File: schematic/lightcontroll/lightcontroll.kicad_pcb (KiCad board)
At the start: 2 copper layers, 99.1 x 99.1 mm, 122 parts, among them J1 SPI1_SS, J10 SPI 5V, J11 3.3V jumper, J12 Header 24X2, J13 Header 24X2, J14 ATX24connector, J15 PWR_JMP, J16 PWR_JMP, J18 DB9_Female_MountingHoles, J19 SK2812_sig, J2 5V Selector, J20 SPI 5V, J21 RJ45_LED_Shielded, J22 Conn_01x03, J23 Conn_01x03, J24 Conn_01x03, J25 Conn_01x03, J26 SK2812_sig, J27 SPI1_MISO, J28 Conn_01x03, J29 Conn_01x03, J3 SPI1_CLK, J30 SK2812_sig, J31 SPI1_MOSI, J32 Conn_01x03, J33 SPI2_SS, J34 SPI2_CLK, J35 SPI2_MISO, J36 SPI2_MOSI, J37 Conn_01x03, J38 Conn_01x03, J39 Conn_01x03, J4 UART/SPI JUMPER, J40 Conn_01x03, J41 Conn_01x02, J5 UART/SPI JUMPER, J6 Conn_02x24_Odd_Even, J7 Conn_02x24_Odd_Even, J8 UART/SPI JUMPER, J9 SPI 5V, Q1 2N7000, U1 74HC14, U10 TXB0104D, U11 74LS123, U12 7402, U13 TXB0104D, U2 MAX13433EESD, U3 MAX13433EESD, U4 74LS123, U5 7402, U6 TXB0104D, U7 MAX232, U8 74LS123, U9 7402

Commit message: save Version 1.0
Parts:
- added J17: Power Connector, TerminalBlock_RND:TerminalBlock_RND_205-00295_1x10_P5.08mm_Horizontal, F.Cu at (16.9, 97.1)
- added J42: Buttonconnector, TerminalBlock_RND:TerminalBlock_RND_205-00291_1x06_P5.08mm_Horizontal, F.Cu at (16.9, 45.2)
- added Q2: 2N2222A, Package_TO_SOT_THT:TO-92_Inline, F.Cu at (29.8, 16.4)
- added Q3: 2N2222A, Package_TO_SOT_THT:TO-92_Inline, F.Cu at (24.3, 16.4)
- added R17: 1K, Resistor_SMD:R_0603_1608Metric_Pad1.05x0.95mm_HandSolder, F.Cu at (25.4, 20.1)
- added R18: 100K, Resistor_SMD:R_0603_1608Metric_Pad1.05x0.95mm_HandSolder, F.Cu at (25.8, 42.1)
- added R19: 100K, Resistor_SMD:R_0603_1608Metric_Pad1.05x0.95mm_HandSolder, F.Cu at (24.3, 42.1)
- added R20: 1K, Resistor_SMD:R_0603_1608Metric_Pad1.05x0.95mm_HandSolder, F.Cu at (23.9, 20.1)
- moved J28 19.6 mm to (20.2, 102.0), turned to 270 degrees
- moved J30 17.6 mm to (41.2, 96.9), turned to 180 degrees
- moved C22 16.8 mm to (37.9, 16.1), turned to 180 degrees
- moved J32 14.4 mm to (20.2, 105.6), turned to 270 degrees
- moved C23 14.1 mm to (37.9, 19.2), turned to 180 degrees
- moved C24 13.0 mm to (37.9, 17.7), turned to 180 degrees
- moved J29 7.20 mm to (20.2, 109.3), turned to 270 degrees
- moved D6 3.56 mm to (24.5, 97.2), turned to 0 degrees
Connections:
- net /12V renamed +12V
- net /3V3 renamed +3V3
- net /5V renamed +5VD
- net /5VSB renamed +5VL
- net /stm32f407_blackboard/PE2 renamed /PE2
- net /stm32f407_blackboard/PE4 renamed /PE4
- net /stm32f407_blackboard/PE5 renamed /PE5
- net /stm32f407_blackboard/PE6 renamed /PE6
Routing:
- net /PE5: track 8.67 -> 48.5 mm, vias 0 -> 2
- net /PE6: track 8.67 -> 45.2 mm, vias 0 -> 2
- net +5VD: track 403.6 -> 432.1 mm
- net Net-(J42-Pad5): track 0.00 -> 23.1 mm
- net /PE2: track 8.67 -> 29.7 mm, vias 0 -> 2
- net /sheet5EBDAB70/SK2812_sig: track 18.5 -> 37.4 mm, vias 0 -> 2
- net /PE4: track 8.67 -> 24.6 mm, vias 0 -> 1
- net /SPI_WS2812_DRIVERS/SK2812_sig: track 55.4 -> 67.7 mm, vias 2 -> 4
- net /5V_UART: track 152.3 -> 163.7 mm
- net /3V3_MC: track 461.2 -> 451.4 mm, vias 14 -> 11
- net Net-(J42-Pad6): track 0.00 -> 8.81 mm
- net Net-(Q2-Pad2): track 0.00 -> 7.48 mm
- net Net-(Q3-Pad2): track 0.00 -> 3.55 mm
- net /stm32f407_blackboard/PB15: track 152.0 -> 154.4 mm, vias 2 -> 3
- net Net-(C44-Pad1): track 14.3 -> 15.9 mm
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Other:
- board text added: "12V"
- board text added: "5V"
- board text added: "GND"
- board text added: "JLCJLCJLCJLC"
- board text added: "Lightcontroller Shield Version 1.0 Designed by: Tibersam All Rights Reserved"
- board text added: "PE2"
- board text added: "PE4"
- board text added: "PE5_5V"
- board text added: "PE6_5V"

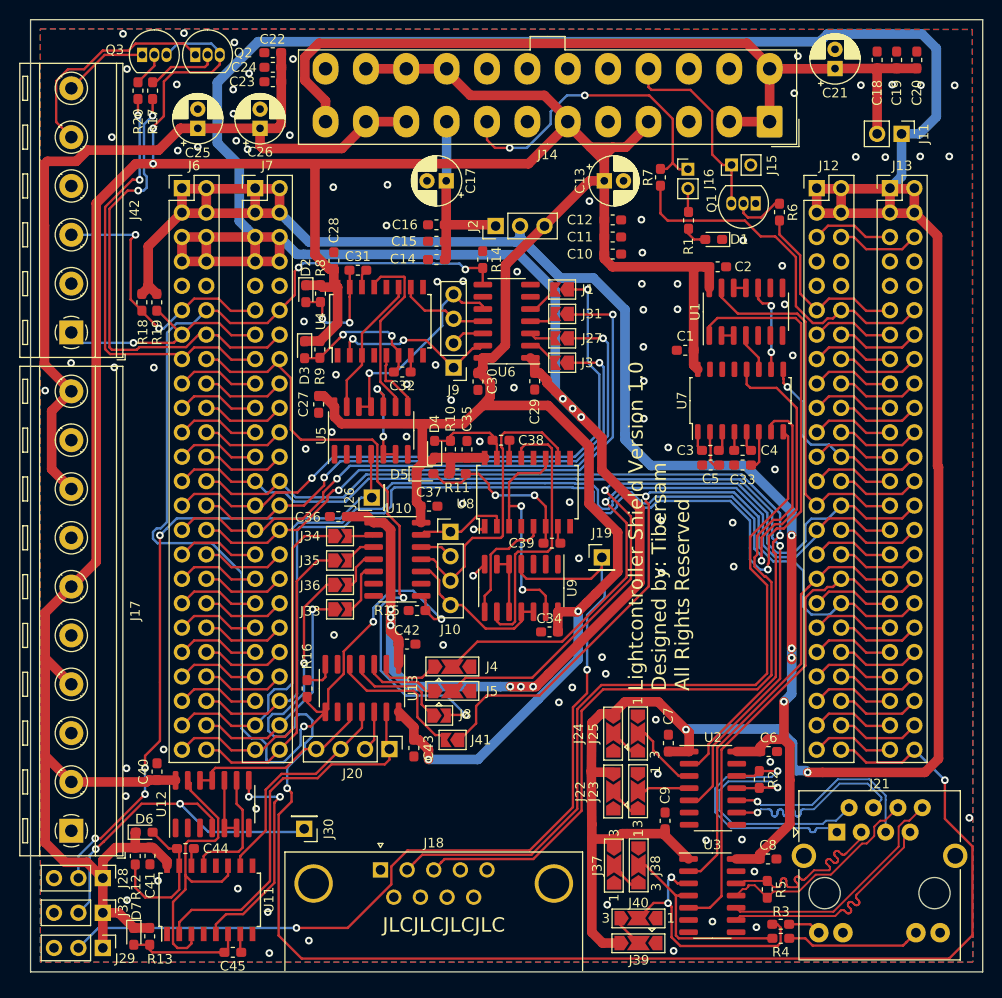
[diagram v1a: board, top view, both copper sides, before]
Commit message: Updated PCB to Revision 2.0
- Added an 2.54mm pin header for second RS232 UART, which was already available in rev 1.0
- Changed all 2.00mm pin header to 2.54mm pin header. This fixes the mistake done in selecting the wrong footprint in rev 1.0
- Corrected schematic and layout of the spi to sk2812 circuits. During testing of previous rev some mistakes where found.
	* the second logical schemitac part of 74ls123 changes meaning of pin 6 and 7 compared to 15 and 14 of the first
	* The vibrator for the one signal needs to be also triggered with every rising edge, so use input A instead of binding it to gnd
	* Use the fourth nand to invert clock signal for a input of one vibrator
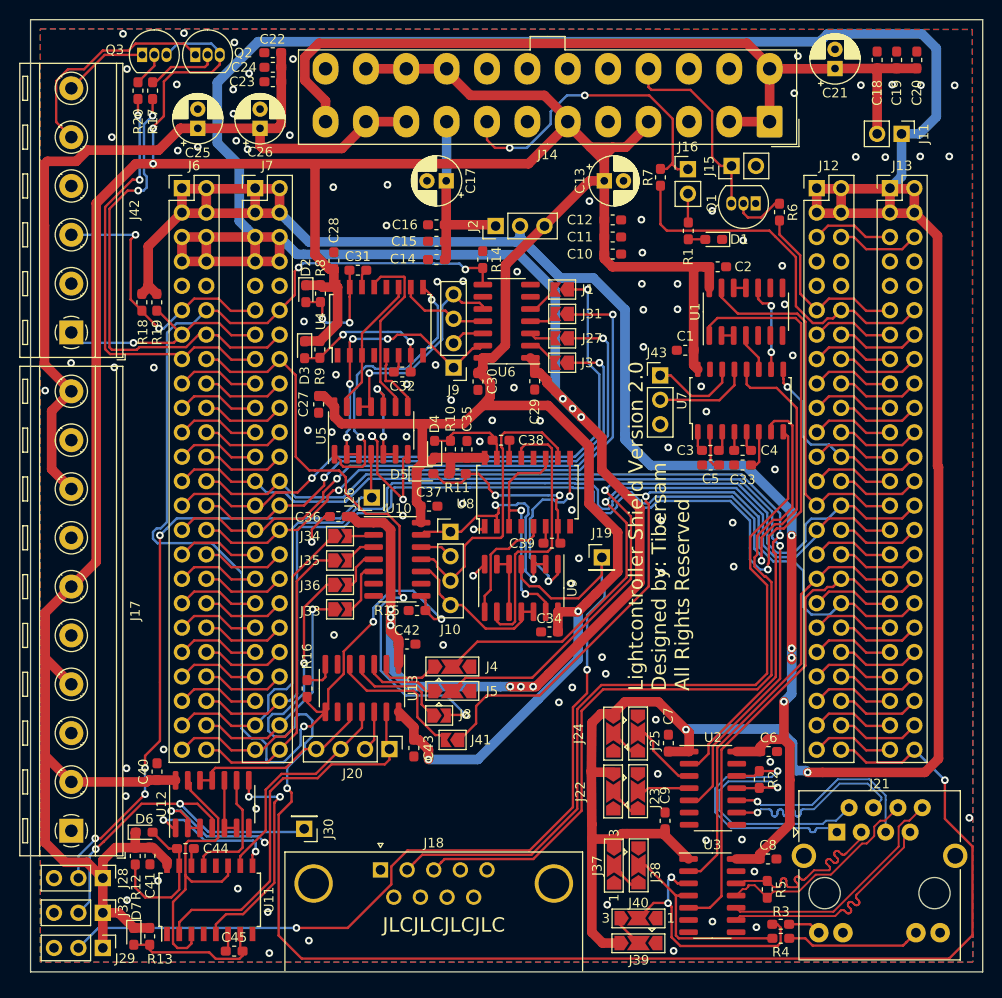
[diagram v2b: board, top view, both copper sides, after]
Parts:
- added J43: Conn_01x03, Connector_PinHeader_2.54mm:PinHeader_1x03_P2.54mm_Vertical, F.Cu at (78.2, 49.7)
- C1, C3, C33, C4, C5: value 1 uF -> 1uF
- C31, C32, C38, C39, C44, C45: value 200 pF -> 200pF
- C9: value 100 nF -> 100nF
- J15, J16: footprint Connector_PinHeader_2.00mm:PinHeader_1x02_P2.00mm_Vertical -> Connector_PinHeader_2.54mm:PinHeader_1x02_P2.54mm_Vertical
- J23, J25, J38: footprint Jumper:SolderJumper-3_P2.0mm_Open_TrianglePad1.0x1.5mm_NumberLabels -> Jumper:SolderJumper-3_P2.0mm_Open_TrianglePad1.0x1.5mm
- R1: value 200 ohm -> 200
- R2: value 120 Ohm -> 120
- R3, R4: value R -> 200
- R5: value R -> 120
- R6: value 10k -> 10K
- moved R1 1.09 mm to (81.1, 34.7)
- moved C45 0.19 mm to (33.9, 109.6), turned to 0 degrees
- moved J15 0.10 mm to (85.6, 27.9)
- turned C32 to 0 degrees
- turned C39 to 0 degrees
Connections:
- U11 pad 6: Net-(C45-Pad2) -> Net-(C45-Pad1)
- U11 pad 7: Net-(C45-Pad1) -> Net-(C45-Pad2)
- U11 pad 9: GNDREF -> Net-(U11-Pad9)
- U12 pad 1: Net-(U12-Pad1) -> Net-(U11-Pad9)
- U12 pad 2: Net-(U12-Pad2) -> /sheet5EBDAB70/CLK5V
- U12 pad 3: Net-(U12-Pad3) -> /sheet5EBDAB70/CLK5V
- U4 pad 6: Net-(C32-Pad2) -> Net-(C32-Pad1)
- U4 pad 7: Net-(C32-Pad1) -> Net-(C32-Pad2)
- U4 pad 9: GNDREF -> Net-(U4-Pad9)
- U5 pad 1: Net-(U5-Pad1) -> Net-(U4-Pad9)
- U5 pad 2: Net-(U5-Pad2) -> /SPI_WS2812_DRIVERS/CLK5V
- U5 pad 3: Net-(U5-Pad3) -> /SPI_WS2812_DRIVERS/CLK5V
- U7 pad 13: Net-(U7-Pad13) -> /UART_RS232/USARTARX
- U7 pad 14: Net-(U7-Pad14) -> /UART_RS232/USARTATX
- U8 pad 6: Net-(C39-Pad2) -> Net-(C39-Pad1)
- U8 pad 7: Net-(C39-Pad1) -> Net-(C39-Pad2)
- U8 pad 9: GNDREF -> Net-(U8-Pad9)
- U9 pad 1: Net-(U9-Pad1) -> Net-(U8-Pad9)
- U9 pad 2: Net-(U9-Pad2) -> /sheet5EBD8EE4/CLK5V
- U9 pad 3: Net-(U9-Pad3) -> /sheet5EBD8EE4/CLK5V
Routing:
- net Net-(U4-Pad9): track 0.00 -> 30.0 mm, vias 0 -> 2
- net Net-(U8-Pad9): track 0.00 -> 19.4 mm, vias 0 -> 2
- net GNDREF: track 6.35 -> 22.9 mm, vias 98 -> 107
- net /sheet5EBD8EE4/CLK5V: track 9.72 -> 25.7 mm, vias 0 -> 2
- net /sheet5EBDAB70/CLK5V: track 40.7 -> 56.6 mm, vias 0 -> 2
- net Net-(U11-Pad9): track 0.00 -> 14.7 mm, vias 0 -> 2
- net /SPI_WS2812_DRIVERS/CLK5V: track 17.9 -> 29.6 mm, vias 2 -> 4
- net /UART_RS232/USARTARX: track 0.00 -> 10.0 mm
- net /UART_RS232/USARTATX: track 0.00 -> 9.29 mm
- net /sheet5EBD8EE4/SK2812_sig: track 97.2 -> 101.7 mm
- net Net-(C39-Pad2): track 18.3 -> 21.3 mm
- net Net-(C45-Pad2): track 12.1 -> 14.7 mm
- net /stm32f407_blackboard/PB13: track 37.0 -> 35.3 mm
- net /stm32f407_blackboard/PC13: track 65.4 -> 64.1 mm
- net Net-(C32-Pad2): track 14.6 -> 15.8 mm
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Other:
- board text added: "Lightcontroller Shield Version 2.0 Designed by: Tibersam All Rights Reserved"
- board text removed: "Lightcontroller Shield Version 1.0 Designed by: Tibersam All Rights Reserved"
